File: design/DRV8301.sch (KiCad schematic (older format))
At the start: 38 parts, among them U2 LM3671-3.3, U3 DRV8301

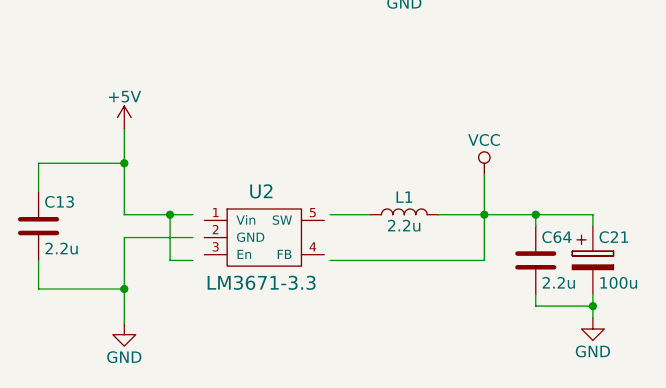
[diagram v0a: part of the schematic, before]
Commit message: Revert "Add ICM-20948 support"
This reverts commit 6973a9f76e2e1207f1c7879789cf7605503054ef.
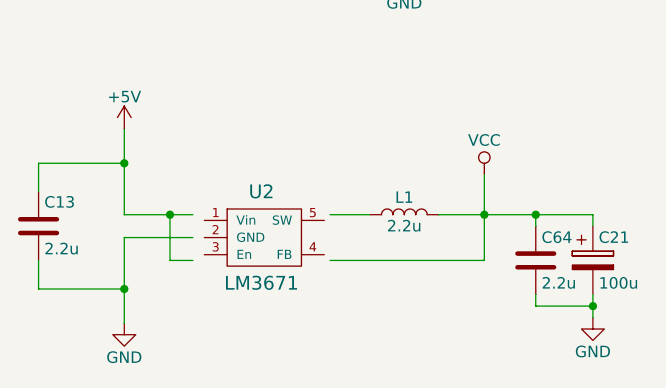
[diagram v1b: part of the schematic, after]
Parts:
- U2: value LM3671-3.3 -> LM3671
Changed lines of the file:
@@
 P 3300 6475
 F 0 "U2" H 3300 6675 60  0000 C CNN
-F 1 "LM3671-3.3" H 3300 6275 60  0000 C CNN
+F 1 "LM3671" H 3300 6275 60  0000 C CNN
 F 2 "TO_SOT_Packages_SMD:SOT-23-5" H 3250 6450 60  0001 C CNN
 F 3 "" H 3250 6450 60  0001 C CNN

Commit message: Design VESC6 plus sch done
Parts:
- removed L1: 2.2u, Inductors_SMD:L_0805, symbol Device:L
- removed U2: LM3671, TO_SOT_Packages_SMD:SOT-23-5, symbol crf_1:LM3671
- added U8: TC2117, TO_SOT_Packages_SMD:SOT-223-3Lead_TabPin2, symbol crf_1:TC2117
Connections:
- wire segments 174 -> 165
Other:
- moved on the sheet: C13, C21, C64
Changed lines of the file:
@@
 $Descr A4 11693 8268
 encoding utf-8
-Sheet 3 7
-Title "VESC 6.4"
-Date "2016-07-07"
+Sheet 6 6
+Title "VESC 6.5"
+Date "2018-02-27"
 Rev "A"
 Comp "Benjamin Vedder"
@@
 $EndComp
 $Comp
-L crf_1:LM3671 U2
-U 1 1 5A970EE4
-P 3300 6475
-F 0 "U2" H 3300 6675 60  0000 C CNN
-F 1 "LM3671" H 3300 6275 60  0000 C CNN
-F 2 "TO_SOT_Packages_SMD:SOT-23-5" H 3250 6450 60  0001 C CNN
-F 3 "" H 3250 6450 60  0001 C CNN
-F 4 "LM3671MF-3.3/NOPB" H 3300 6775 50  0001 C CNN "manf#"
-	1    3300 6475
-	1    0    0    -1
-$EndComp
-$Comp
-L power:GND #PWR059
-U 1 1 5A9712C4
-P 2700 6850
-F 0 "#PWR059" H 2700 6600 50  0001 C CNN
-F 1 "GND" H 2700 6700 50  0000 C CNN
-F 2 "" H 2700 6850 50  0001 C CNN
-F 3 "" H 2700 6850 50  0001 C CNN
-	1    2700 6850
-	1    0    0    -1
-$EndComp
-$Comp
 L power:+5V #PWR060
 U 1 1 5A971545
-P 2700 6000
-F 0 "#PWR060" H 2700 5850 50  0001 C CNN
-F 1 "+5V" H 2700 6140 50  0000 C CNN
-F 2 "" H 2700 6000 50  0001 C CNN
-F 3 "" H 2700 6000 50  0001 C CNN
-	1    2700 6000
+P 2700 6150
+F 0 "#PWR060" H 2700 6000 50  0001 C CNN
+F 1 "+5V" H 2700 6290 50  0000 C CNN
+F 2 "" H 2700 6150 50  0001 C CNN
+F 3 "" H 2700 6150 50  0001 C CNN
+	1    2700 6150
 	1    0    0    -1
 $EndComp
@@
 L power:VCC #PWR061
 U 1 1 5A971A5F
-P 4275 6200
-F 0 "#PWR061" H 4275 6050 50  0001 C CNN
-F 1 "VCC" H 4275 6350 50  0000 C CNN
-F 2 "" H 4275 6200 50  0001 C CNN
-F 3 "" H 4275 6200 50  0001 C CNN
-	1    4275 6200
-	1    0    0    -1
-$EndComp
-$Comp
-L Device:C C13
-U 1 1 5A972EAC
-P 2325 6425
-F 0 "C13" H 2350 6500 50  0000 L BNN
-F 1 "2.2u" H 2350 6325 50  0000 L CNN
-F 2 "Capacitors_SMD:C_0603" H 2325 6425 60  0001 C CNN
-F 3 "" H 2325 6425 60  0001 C CNN
-F 4 "C1608X5R1C225K080AB" H 2350 6600 50  0001 C CNN "manf#"
-	1    2325 6425
-	1    0    0    -1
-$EndComp
-$Comp
-L Device:L L1
-U 1 1 5A974894
-P 3925 6375
-F 0 "L1" V 4000 6375 50  0000 C CNN
-F 1 "2.2u" V 3875 6375 50  0000 C CNN
-F 2 "Inductors_SMD:L_0805" H 3925 6375 50  0001 C CNN
-F 3 "" H 3925 6375 50  0001 C CNN
-F 4 "74479275222" H 4000 6475 50  0001 C CNN "manf#"
-	1    3925 6375
-	0    -1   -1   0
-$EndComp
-$Comp
-L Device:C C64
-U 1 1 5A9748A2
-P 4500 6575
-F 0 "C64" H 4525 6675 50  0000 L CNN
-F 1 "2.2u" H 4525 6475 50  0000 L CNN
-F 2 "Capacitors_SMD:C_0603" H 4538 6425 50  0001 C CNN
-F 3 "" H 4500 6575 50  0001 C CNN
-F 4 "C1608X5R1C225K080AB" H 4525 6775 50  0001 C CNN "manf#"
-	1    4500 6575
-	1    0    0    -1
-$EndComp
-$Comp
-L Device:CP C21
-U 1 1 5A9748A8
-P 4750 6575
-F 0 "C21" H 4775 6675 50  0000 L CNN
-F 1 "100u" H 4775 6475 50  0000 L CNN
-F 2 "Capacitors_Tantalum_SMD:CP_Tantalum_Case-A_EIA-3216-18_Reflow" H 4788 6425 50  0001 C CNN
-F 3 "" H 4750 6575 50  0001 C CNN
-F 4 "TLJA107M006R0500" H 4775 6775 50  0001 C CNN "manf#"
-	1    4750 6575
-	1    0    0    -1
-$EndComp
-$Comp
-L power:GND #PWR062
-U 1 1 5A9748B1
-P 4750 6825
-F 0 "#PWR062" H 4750 6575 50  0001 C CNN
-F 1 "GND" H 4750 6675 50  0000 C CNN
-F 2 "" H 4750 6825 50  0001 C CNN
-F 3 "" H 4750 6825 50  0001 C CNN
-	1    4750 6825
+P 3925 6200
+F 0 "#PWR061" H 3925 6050 50  0001 C CNN
+F 1 "VCC" H 3925 6350 50  0000 C CNN
+F 2 "" H 3925 6200 50  0001 C CNN
+F 3 "" H 3925 6200 50  0001 C CNN
+	1    3925 6200
 	1    0    0    -1
 $EndComp
@@
 	8875 5625 8875 5475
 Wire Wire Line
-	2700 6375 2900 6375
-Wire Wire Line
-	2700 6000 2700 6150
-Wire Wire Line
-	3000 6575 2900 6575
-Wire Wire Line
-	2900 6575 2900 6375
-Wire Wire Line
-	3000 6475 2700 6475
-Wire Wire Line
-	2700 6475 2700 6700
-Wire Wire Line
-	2325 6150 2325 6275
-Wire Wire Line
-	2325 6150 2700 6150
-Wire Wire Line
-	2325 6575 2325 6700
-Wire Wire Line
-	2325 6700 2700 6700
-Wire Wire Line
-	3600 6375 3775 6375
-Wire Wire Line
-	4075 6375 4275 6375
-Wire Wire Line
-	4500 6425 4500 6375
-Wire Wire Line
-	4750 6725 4750 6775
-Wire Wire Line
-	4500 6725 4500 6775
-Wire Wire Line
-	4275 6575 3600 6575
-Wire Wire Line
-	4275 6200 4275 6375
-Wire Wire Line
-	4750 6375 4750 6425
-Wire Wire Line
-	4500 6775 4750 6775
+	3925 6200 3925 6375
 Wire Wire Line
 	2900 1375 2900 1500
@@
 Wire Wire Line
 	8875 5475 9075 5475
-Wire Wire Line
-	2900 6375 3000 6375
-Wire Wire Line
-	2700 6150 2700 6375
-Wire Wire Line
-	2700 6700 2700 6850
-Wire Wire Line
-	4500 6375 4750 6375
-Wire Wire Line
-	4750 6775 4750 6825
-Wire Wire Line
-	4275 6375 4500 6375
-Wire Wire Line
-	4275 6375 4275 6575
 Connection ~ 3675 2125
 Connection ~ 3675 900
@@
 Connection ~ 8875 4950
 Connection ~ 8875 5475
-Connection ~ 2900 6375
-Connection ~ 2700 6150
-Connection ~ 2700 6700
-Connection ~ 4500 6375
-Connection ~ 4750 6775
-Connection ~ 4275 6375
 NoConn ~ 4225 2325
 NoConn ~ 4225 2425
@@
 NoConn ~ 4225 4525
 NoConn ~ 5825 2125
+Wire Wire Line
+	2700 6375 2950 6375
+Wire Wire Line
+	2700 6150 2700 6375
+Connection ~ 2700 6375
+Wire Wire Line
+	2700 6375 2700 6425
+$Comp
+L Device:C C13
+U 1 1 5A972EAC
+P 2700 6575
+F 0 "C13" H 2725 6650 50  0000 L BNN
+F 1 "2.2u" H 2725 6475 50  0000 L CNN
+F 2 "Capacitors_SMD:C_0603" H 2700 6575 60  0001 C CNN
+F 3 "" H 2700 6575 60  0001 C CNN
+F 4 "C1608X5R1C225K080AB" H 2725 6750 50  0001 C CNN "manf#"
+	1    2700 6575
+	1    0    0    -1
+$EndComp
+Wire Wire Line
+	2700 6775 2700 6725
+Wire Wire Line
+	3350 6675 3350 6775
+Connection ~ 3350 6775
+Wire Wire Line
+	2700 6775 3350 6775
+Wire Wire Line
+	3350 6775 4150 6775
+Connection ~ 4150 6775
+Connection ~ 4400 6775
+Connection ~ 4150 6375
+Wire Wire Line
+	4400 6775 4400 6825
+Wire Wire Line
+	4150 6375 4400 6375
+Wire Wire Line
+	4150 6775 4400 6775
+Wire Wire Line
+	4400 6375 4400 6425
+Wire Wire Line
+	4150 6725 4150 6775
+Wire Wire Line
+	4400 6725 4400 6775
+Wire Wire Line
+	4150 6425 4150 6375
+$Comp
+L power:GND #PWR062
+U 1 1 5A9748B1
+P 4400 6825
+F 0 "#PWR062" H 4400 6575 50  0001 C CNN
+F 1 "GND" H 4400 6675 50  0000 C CNN
+F 2 "" H 4400 6825 50  0001 C CNN
+F 3 "" H 4400 6825 50  0001 C CNN
+	1    4400 6825
+	1    0    0    -1
+$EndComp
+$Comp
+L Device:CP C21
+U 1 1 5A9748A8
+P 4400 6575
+F 0 "C21" H 4425 6675 50  0000 L CNN
+F 1 "100u" H 4425 6475 50  0000 L CNN
+F 2 "Capacitors_Tantalum_SMD:CP_Tantalum_Case-A_EIA-3216-18_Reflow" H 4438 6425 50  0001 C CNN
+F 3 "" H 4400 6575 50  0001 C CNN
+F 4 "TLJA107M006R0500" H 4425 6775 50  0001 C CNN "manf#"
+	1    4400 6575
+	1    0    0    -1
+$EndComp
+$Comp
+L Device:C C64
+U 1 1 5A9748A2
+P 4150 6575
+F 0 "C64" H 4175 6675 50  0000 L CNN
+F 1 "2.2u" H 4175 6475 50  0000 L CNN
+F 2 "Capacitors_SMD:C_0603" H 4188 6425 50  0001 C CNN
+F 3 "" H 4150 6575 50  0001 C CNN
+F 4 "C1608X5R1C225K080AB" H 4175 6775 50  0001 C CNN "manf#"
+	1    4150 6575
+	1    0    0    -1
+$EndComp
+Wire Wire Line
+	3750 6375 3925 6375
+Connection ~ 3925 6375
+Wire Wire Line
+	3925 6375 4150 6375
+$Comp
+L crf_1:TC2117 U8
+U 1 1 5DFAD245
+P 3350 6425
+F 0 "U8" H 3350 6725 60  0000 C CNN
+F 1 "TC2117" H 3350 6625 60  0000 C CNN
+F 2 "TO_SOT_Packages_SMD:SOT-223-3Lead_TabPin2" H 3350 6425 60  0001 C CNN
+F 3 "" H 3350 6425 60  0000 C CNN
+	1    3350 6425
+	1    0    0    -1
+$EndComp
 $EndSCHEMATC

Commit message: assign component footprint
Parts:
- U8: footprint TO_SOT_Packages_SMD:SOT-223-3Lead_TabPin2 -> TO_SOT_Packages_SMD:SOT-223
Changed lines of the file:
@@
 F 0 "U8" H 3350 6725 60  0000 C CNN
 F 1 "TC2117" H 3350 6625 60  0000 C CNN
-F 2 "TO_SOT_Packages_SMD:SOT-223-3Lead_TabPin2" H 3350 6425 60  0001 C CNN
+F 2 "TO_SOT_Packages_SMD:SOT-223" H 3350 6425 60  0001 C CNN
 F 3 "" H 3350 6425 60  0000 C CNN
 	1    3350 6425

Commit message: Update layout
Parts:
- D4: footprint Diodes_SMD:D_SMB -> Diodes_SMD:D_SMA
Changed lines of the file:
@@
 F 0 "D4" H 6800 2780 50  0000 L CNN
 F 1 "DIODE" H 6750 2620 50  0000 L CNN
-F 2 "Diodes_SMD:D_SMB" V 6850 2700 50  0001 C CNN
+F 2 "Diodes_SMD:D_SMA" V 6850 2700 50  0001 C CNN
 F 3 "" V 6850 2700 50  0001 C CNN
 F 4 "NTS260ESFT3G" H 6800 2880 50  0001 C CNN "manf#"
